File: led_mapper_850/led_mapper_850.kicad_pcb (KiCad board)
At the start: 2 copper layers, 530 parts, among them J1 Conn_02x12_Top_Bottom

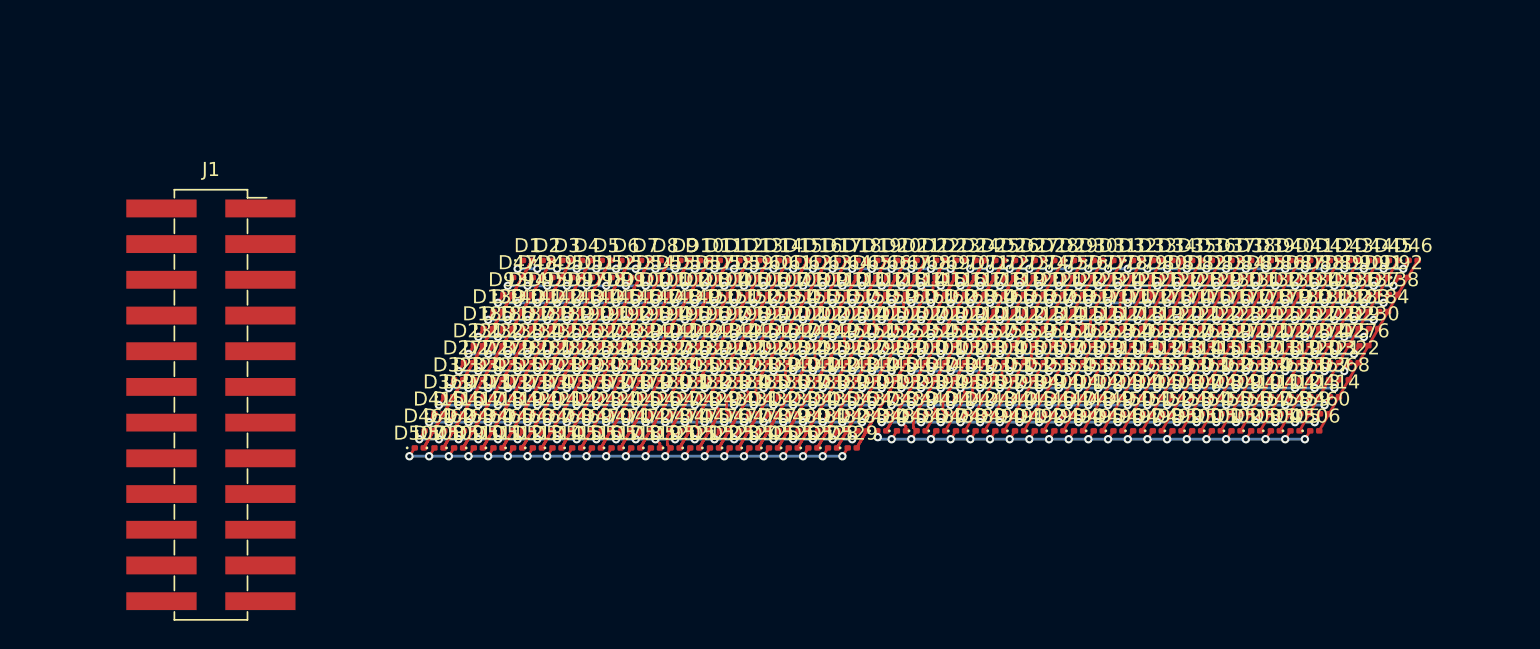
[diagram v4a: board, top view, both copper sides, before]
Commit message: complete wiring after rotating leds
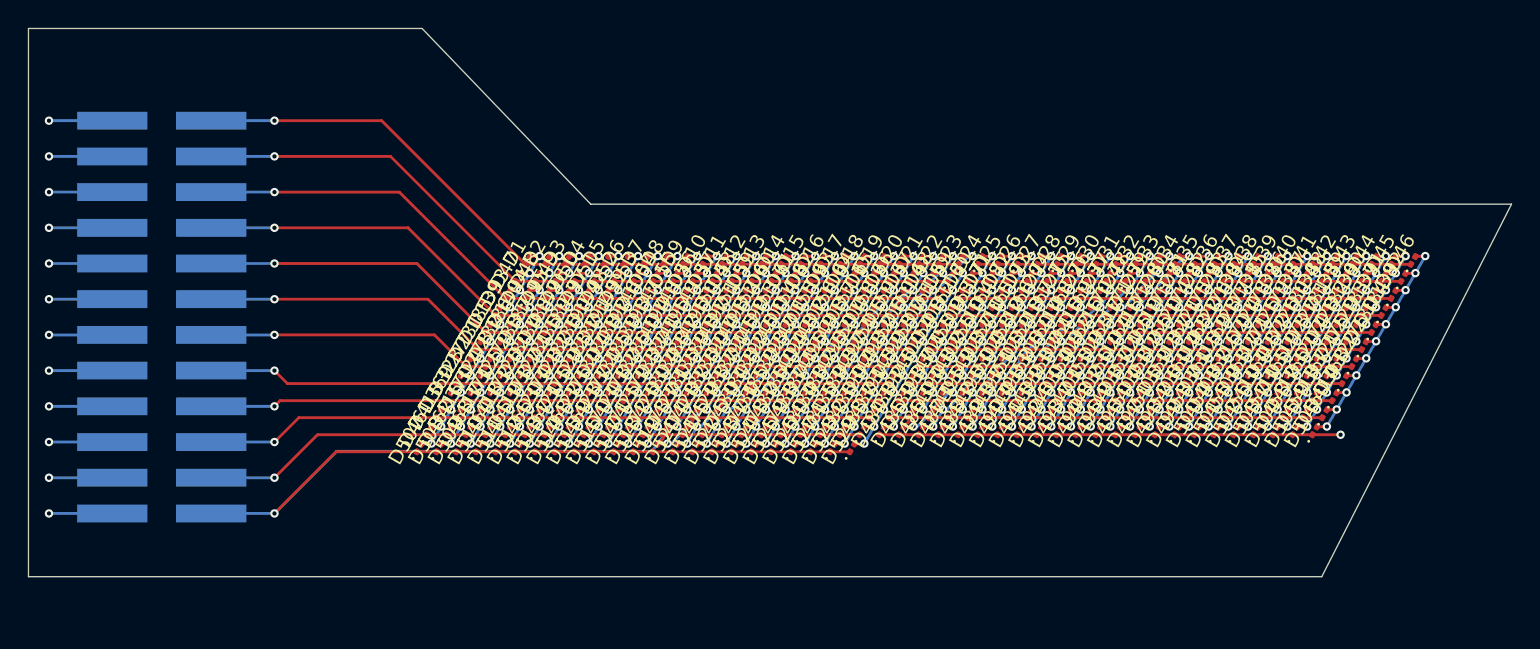
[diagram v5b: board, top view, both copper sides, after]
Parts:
- J1: moved to B.Cu
- moved J1 7.15 mm to (-26.0, 4.03)
- turned D1 to 60 degrees
- turned D10 to 60 degrees
- turned D100 to 60 degrees
- turned D101 to 60 degrees
- turned D102 to 60 degrees
- turned D103 to 60 degrees
- turned D104 to 60 degrees
- turned D105 to 60 degrees
- turned D106 to 60 degrees
- turned D107 to 60 degrees
- turned D108 to 60 degrees
- turned D109 to 60 degrees
- turned D11 to 60 degrees
- turned D110 to 60 degrees
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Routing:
- net /P02: track 103.8 -> 181.0 mm, vias 23 -> 24
- net /P12: track 91.2 -> 167.3 mm
- net /P11: track 91.2 -> 165.5 mm
- net /P10: track 91.2 -> 163.3 mm
- net /P09: track 91.2 -> 160.0 mm
- net /P08: track 91.2 -> 158.0 mm
- net /P07: track 91.2 -> 154.7 mm
- net /P13: track 90.4 -> 153.3 mm
- net /P06: track 91.2 -> 153.4 mm
- net /P05: track 91.2 -> 150.6 mm
- net /P04: track 91.2 -> 148.1 mm
- net /P01: track 58.8 -> 112.0 mm, vias 0 -> 24
- net /P23: track 87.0 -> 135.6 mm
- net /P22: track 88.4 -> 134.4 mm
- net /P21: track 88.4 -> 133.1 mm
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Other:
- board outline added: 105.5 x 39 mm
- copper layers 2 -> 4
